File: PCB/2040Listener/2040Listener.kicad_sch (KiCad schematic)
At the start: 23 parts, among them J1 USB_B_Micro, J2 Conn_01x02, U1 NCP1117-3.3_SOT223, U2 BY25Q16AWTIG(R), U3 RP2040

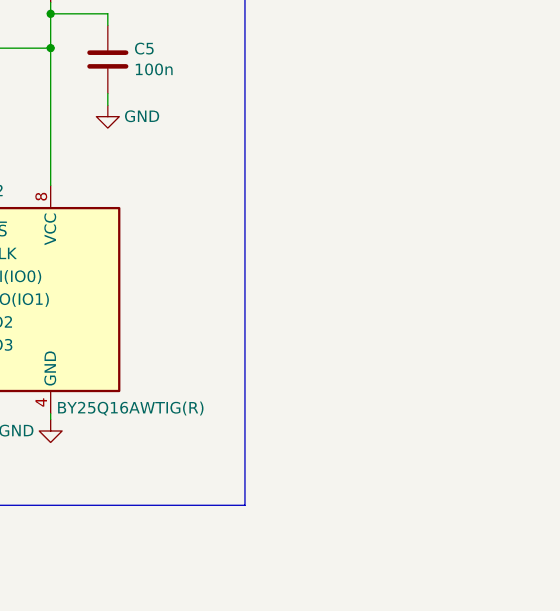
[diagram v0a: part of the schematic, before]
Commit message: change to 0805
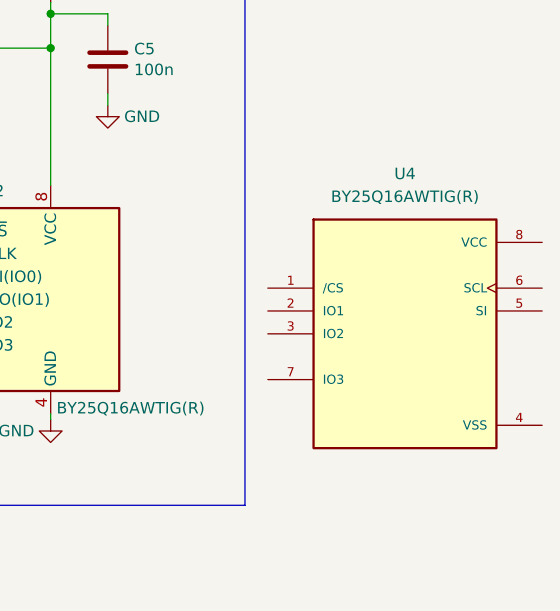
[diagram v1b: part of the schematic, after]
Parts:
- added U4: BY25Q16AWTIG(R), symbol SymbolLibrary:BY25Q16AWTIG(R)
- C10, C11, C12, C13, C14, C15, C16, C5, C6, C7, C8, C9: footprint Capacitor_SMD:C_0402_1005Metric -> Capacitor_SMD:C_0805_2012Metric
- R1, R2, R3, R4: footprint Resistor_SMD:R_0402_1005Metric -> Resistor_SMD:R_0805_2012Metric
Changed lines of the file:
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@@
 			)
 		)
-		(property "Footprint" "Resistor_SMD:R_0402_1005Metric"
+		(property "Footprint" "Resistor_SMD:R_0805_2012Metric"
 			(at 256.032 34.29 90)
 			(effects
@@
 			)
 		)
-		(property "Footprint" "Resistor_SMD:R_0402_1005Metric"
+		(property "Footprint" "Resistor_SMD:R_0805_2012Metric"
 			(at 242.57 47.752 90)
 			(effects
@@
 			)
 		)
-		(property "Footprint" "Capacitor_SMD:C_0402_1005Metric"
+		(property "Footprint" "Capacitor_SMD:C_0805_2012Metric"
 			(at 299.4152 34.29 0)
 			(effects
@@
 			)
 		)
-		(property "Footprint" "Resistor_SMD:R_0402_1005Metric"
+		(property "Footprint" "Resistor_SMD:R_0805_2012Metric"
 			(at 144.78 56.642 90)
 			(effects
@@
 			)
 		)
-		(property "Footprint" "Resistor_SMD:R_0402_1005Metric"
+		(property "Footprint" "Resistor_SMD:R_0805_2012Metric"
 			(at 144.78 64.262 90)
 			(effects
@@
 			)
 		)
-		(property "Footprint" "Capacitor_SMD:C_0402_1005Metric"
+		(property "Footprint" "Capacitor_SMD:C_0805_2012Metric"
 			(at 124.1552 31.75 0)
 			(effects
@@
 			)
 		)
-		(property "Footprint" "Capacitor_SMD:C_0402_1005Metric"
+		(property "Footprint" "Capacitor_SMD:C_0805_2012Metric"
 			(at 135.5852 31.75 0)
 			(effects
@@
 			)
 		)
-		(property "Footprint" "Capacitor_SMD:C_0402_1005Metric"
+		(property "Footprint" "Capacitor_SMD:C_0805_2012Metric"
 			(at 147.0152 31.75 0)
 			(effects
@@
 			)
 		)
-		(property "Footprint" "Capacitor_SMD:C_0402_1005Metric"
+		(property "Footprint" "Capacitor_SMD:C_0805_2012Metric"
 			(at 158.4452 31.75 0)
 			(effects
@@
 			)
 		)
-		(property "Footprint" "Capacitor_SMD:C_0402_1005Metric"
+		(property "Footprint" "Capacitor_SMD:C_0805_2012Metric"
 			(at 169.8752 31.75 0)
 			(effects
@@
 			)
 		)
-		(property "Footprint" "Capacitor_SMD:C_0402_1005Metric"
+		(property "Footprint" "Capacitor_SMD:C_0805_2012Metric"
 			(at 181.3052 31.75 0)
 			(effects
@@
 			)
 		)
-		(property "Footprint" "Capacitor_SMD:C_0402_1005Metric"
+		(property "Footprint" "Capacitor_SMD:C_0805_2012Metric"
 			(at 192.7352 31.75 0)
 			(effects
@@
 			)
 		)
-		(property "Footprint" "Capacitor_SMD:C_0402_1005Metric"
+		(property "Footprint" "Capacitor_SMD:C_0805_2012Metric"
 			(at 58.1152 31.75 0)
 			(effects
@@
 			)
 		)
-		(property "Footprint" "Capacitor_SMD:C_0402_1005Metric"
+		(property "Footprint" "Capacitor_SMD:C_0805_2012Metric"
 			(at 69.5452 31.75 0)
 			(effects
@@
 			)
 		)
-		(property "Footprint" "Capacitor_SMD:C_0402_1005Metric"
+		(property "Footprint" "Capacitor_SMD:C_0805_2012Metric"
 			(at 69.5452 46.99 0)
 			(effects
@@
 			)
 		)
-		(property "Footprint" "Capacitor_SMD:C_0402_1005Metric"
+		(property "Footprint" "Capacitor_SMD:C_0805_2012Metric"
 			(at 124.1552 46.99 0)
 			(effects
@@
 					(unit 1)
 				)
+			)
+		)
+	)
+	(symbol
+		(lib_id "SymbolLibrary:BY25Q16AWTIG(R)")
+		(at 331.47 60.96 0)
+		(unit 1)
+		(exclude_from_sim no)
+		(in_bom yes)
+		(on_board yes)
+		(dnp no)
+		(fields_autoplaced yes)
+		(property "Reference" "U4"
+			(at 331.47 43.18 0)
+			(effects
+				(font
+					(size 1.27 1.27)
+				)
+			)
+		)
+		(property "Value" "BY25Q16AWTIG(R)"
+			(at 331.47 45.72 0)
+			(effects
+				(font
+					(size 1.27 1.27)
+				)
+			)
+		)
+		(property "Footprint" ""
+			(at 331.47 60.96 0)
+			(effects
+				(font
+					(size 1.27 1.27)
+				)
+				(justify bottom)
+				(hide yes)
+			)
+		)
+		(property "Datasheet" ""
+			(at 331.47 60.96 0)
+			(effects
+				(font
+					(size 1.27 1.27)
+				)
+				(hide yes)
+			)
+		)
+		(property "Description" ""
+			(at 331.47 60.96 0)
+			(effects
+				(font
+					(size 1.27 1.27)
+				)
+				(hide yes)
+			)
+		)
+		(property "MAXIMUM_PACKAGE_HEIGHT" ""
+			(at 331.47 60.96 0)
+			(effects
+				(font
+					(size 1.27 1.27)
+				)
+				(justify bottom)
+				(hide yes)
+			)
+		)
+		(property "CREATOR" ""
+			(at 331.47 60.96 0)
+			(effects
+				(font
+					(size 1.27 1.27)
+				)
+				(justify bottom)
+				(hide yes)
+			)
+		)
+		(property "STANDARD" ""
+			(at 331.47 60.96 0)
+			(effects
+				(font
+					(size 1.27 1.27)
+				)
+				(justify bottom)
+				(hide yes)
+			)
+		)
+		(property "PARTREV" ""
+			(at 331.47 60.96 0)
+			(effects
+				(font
+					(size 1.27 1.27)
+				)
+				(justify bottom)
+				(hide yes)
+			)
+		)
+		(property "VERIFIER" ""
+			(at 331.47 60.96 0)
+			(effects
+				(font
+					(size 1.27 1.27)
+				)
+				(justify bottom)
+				(hide yes)
+			)
+		)
+		(property "MANUFACTURER" ""
+			(at 331.47 60.96 0)
+			(effects
+				(font
+					(size 1.27 1.27)
+				)
+				(justify bottom)
+				(hide yes)
+			)
+		)
+		(pin "3"
+		)
+		(pin "4"
+		)
+		(pin "1"
+		)
+		(pin "7"
+		)
+		(pin "6"
+		)
+		(pin "8"
+		)
+		(pin "2"
+		)
+		(pin "5"
+		)
+		(instances
+			(project ""
+				(path "/a808e31f-6f6f-4c04-a547-e5c681d45c47"
+					(reference "U4")
+					(unit 1)
+				)

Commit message: update pcb, symbols
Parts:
- removed J1: USB_B_Micro, RP2040_minimal:USB_Micro-B_Amphenol_10103594-0001LF_Horizontal_modified, symbol Connector:USB_B_Micro
- added C13: 15p, Diode_SMD:D_0805_2012Metric, symbol Device:C
- added C14: 15p, Capacitor_SMD:C_0402_1005Metric, symbol Device:C
- added C9: 10u, Capacitor_SMD:C_0805_2012Metric, symbol Device:C
- added J1: CONN4_292303_SOCKET, Library:CONN4_292303_TEC, symbol SymbolLibrary:CONN RCPT TYPEA 4POS R/A
- added J2: USB-AP-S-RA-PLUG, Library:CONN_USB-AP-S-RA-SMT_ADM, symbol SymbolLibrary:USB-AP-S-RA-SMT
- added R5: 1k, Resistor_SMD:R_0805_2012Metric, symbol Device:R
- added Y1: ABM8-272-T3, Crystal:Crystal_SMD_3225-4Pin_3.2x2.5mm, symbol Device:Crystal_GND24
- renumbered C6 to C1, C14 to C10, C15 to C11, C16 to C12, C1 to C15, C4 to C16, C5 to C17, C7 to C2, C8 to C3, C9 to C4, C10 to C5, C11 to C6, C12 to C7, C13 to C8, J2 to J3, R3 to R1, R4 to R2, R1 to R3, R2 to R4, U3 to U1, U1 to U2, U2 to U3
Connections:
- net +3V3: now also C9.1
- net GND: now also C13.2, C14.2, C9.2, J1.4 (GND), J2.4 (GND), Y1.2, Y1.4
- net GPIO0: now also J1.3 (D+)
- net GPIO1: now also J1.2 (D-)
- net USB_D+: now also J2.3 (D+)
- net USB_D-: now also J2.2 (D-)
- net VBUS: now also J1.1 (5V), J2.1 (5V)
- net XIN: now also C13.1, Y1.1
- net XOUT: now also R5.1
- net GPIO10: no longer names the net of U1.13 (GPIO10)
- net GPIO11: no longer names the net of U1.14 (GPIO11)
- net GPIO12: no longer names the net of U1.15 (GPIO12)
- net GPIO13: no longer names the net of U1.16 (GPIO13)
- net GPIO14: no longer names the net of U1.17 (GPIO14)
- net GPIO15: no longer names the net of U1.18 (GPIO15)
- net GPIO16: no longer names the net of U1.27 (GPIO16)
- net GPIO17: no longer names the net of U1.28 (GPIO17)
- net GPIO18: no longer names the net of U1.29 (GPIO18)
- net GPIO19: no longer names the net of U1.30 (GPIO19)
- net GPIO20: no longer names the net of U1.31 (GPIO20)
- net GPIO21: no longer names the net of U1.32 (GPIO21)
- net GPIO22: no longer names the net of U1.34 (GPIO22)
- net GPIO23: no longer names the net of U1.35 (GPIO23)
- net GPIO24: no longer names the net of U1.36 (GPIO24)
- net GPIO25: no longer names the net of U1.37 (GPIO25)
- net GPIO26_ADC0: no longer names the net of U1.38 (GPIO26_ADC0)
- net GPIO27_ADC1: no longer names the net of U1.39 (GPIO27_ADC1)
- net GPIO28_ADC2: no longer names the net of U1.40 (GPIO28_ADC2)
- net GPIO29_ADC3: no longer names the net of U1.41 (GPIO29_ADC3)
- net GPIO5: no longer names the net of U1.7 (GPIO5)
- net GPIO6: no longer names the net of U1.8 (GPIO6)
- net GPIO7: no longer names the net of U1.9 (GPIO7)
- net GPIO8: no longer names the net of U1.11 (GPIO8)
- net GPIO9: no longer names the net of U1.12 (GPIO9)
- new net: C14.1, R5.2, Y1.3
- no-connect marks 1 -> 0
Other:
- note added: "Crystal"
- note added: "USB"
- moved on the sheet: C15, C16, U2

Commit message: routing
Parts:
- removed J3: Conn_01x02, Connector_PinHeader_2.54mm:PinHeader_1x02_P2.54mm_Vertical, symbol Connector_Generic:Conn_01x02
- added R6: 1k, Resistor_SMD:R_0805_2012Metric, symbol Device:R
- added R7, R8: 27, Resistor_SMD:R_0805_2012Metric, symbol Device:R
- added SW1, SW2: PTS815 SJM 250 SMTR LFS, Library:SW4_PTS815 SJM 250 SMTR LFS_CNK, symbol SymbolLibrary:PTS815_SJM_250_SMTR_LFS
- U1: footprint RP2040_minimal:RP2040-QFN-56 -> Library:RP2040-QFN-56
- U4: footprint (none) -> Library:SOIC127P600X175-8N
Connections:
- net +3V3: now also SW2.4
- net GND: now also R6.2, SW1.3
- net GPIO0: now also R7.1; no longer U1.2 (GPIO0)
- net GPIO1: now also R8.1; no longer U1.3 (GPIO1)
- net GPIO17: now reaches U1.28 (GPIO17)
- net GPIO17: now also SW2.2
- net GPIO2: no longer names the net of U1.4 (GPIO2)
- net GPIO3: no longer names the net of U1.5 (GPIO3)
- net GPIO4: no longer names the net of U1.6 (GPIO4)
- net ~{USB_BOOT}: no longer names the net of R3.2
- net ~{USB_BOOT}: now also SW1.2
- new net: R7.2, U1.2 (GPIO0)
- new net: R8.2, U1.3 (GPIO1)
- new net: R6.1, SW2.1
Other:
- note added: "CDC Toggle"
- moved on the sheet: R3, R4

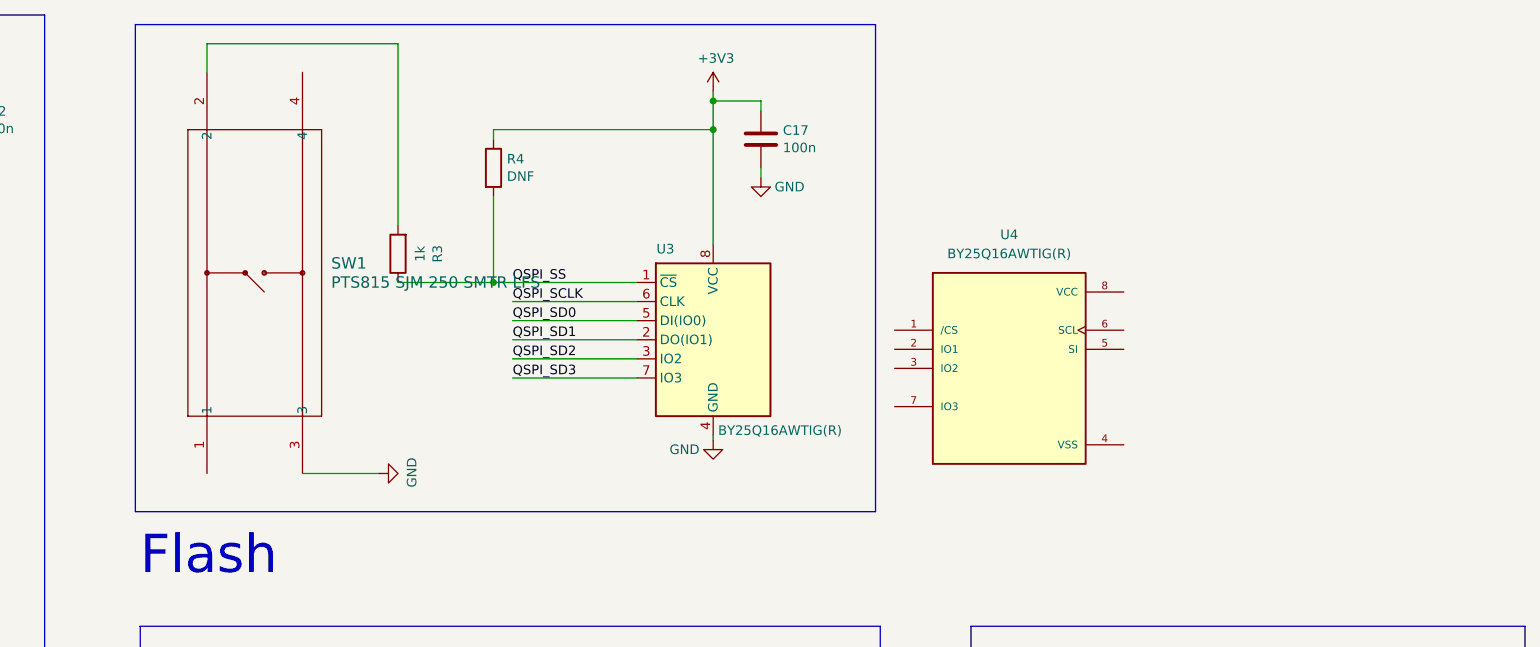
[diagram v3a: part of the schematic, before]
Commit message: reposition elements for better routing
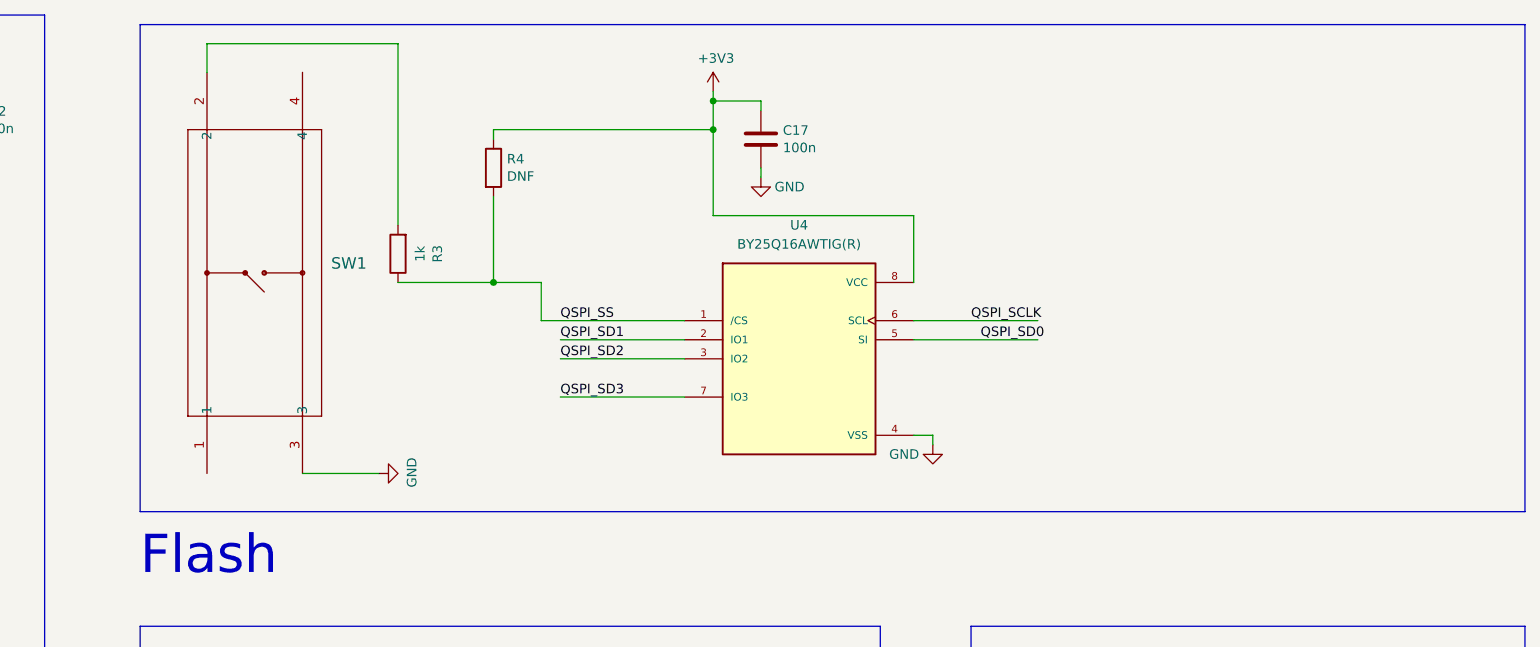
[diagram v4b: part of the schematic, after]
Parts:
- removed U3: BY25Q16AWTIG(R), Package_SO:SOIC-8_5.23x5.23mm_P1.27mm, symbol Memory_Flash:W25Q128JVS
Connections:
- net +3V3: now also U4.8 (VCC)
- net GND: now also U4.4 (VSS)
- net QSPI_SCLK: now also U4.6 (SCL)
- net QSPI_SD0: now also U4.5 (SI)
- net QSPI_SD1: now also U4.2 (IO1)
- net QSPI_SD2: now also U4.3 (IO2)
- net QSPI_SD3: now also U4.7 (IO3)
- net QSPI_SS: now also U4.1 (/CS)
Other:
- moved on the sheet: U4
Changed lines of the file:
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@@
 	(paper "A3")
 	(rectangle
-		(start 215.265 15.24)
-		(end 313.69 80.01)
+		(start 215.9 15.24)
+		(end 400.05 80.01)
 		(stroke
 			(width 0)
@@
 	(wire
 		(pts
-			(xy 281.94 59.69) (xy 265.43 59.69)
+			(xy 288.29 59.69) (xy 271.78 59.69)
 		)
 		(stroke
@@
 	(wire
 		(pts
-			(xy 265.43 52.07) (xy 281.94 52.07)
+			(xy 321.31 69.85) (xy 318.77 69.85)
 		)
 		(stroke
@@
 	(wire
 		(pts
-			(xy 281.94 57.15) (xy 265.43 57.15)
+			(xy 288.29 57.15) (xy 271.78 57.15)
 		)
 		(stroke
@@
 	(wire
 		(pts
+			(xy 318.77 54.61) (xy 335.28 54.61)
+		)
+		(stroke
+			(width 0)
+			(type default)
+		)
+	)
+	(wire
+		(pts
 			(xy 237.49 115.57) (xy 247.65 115.57)
 		)
@@
 	(wire
 		(pts
-			(xy 262.89 49.53) (xy 281.94 49.53)
+			(xy 269.24 54.61) (xy 288.29 54.61)
 		)
 		(stroke
@@
 	(wire
 		(pts
+			(xy 292.1 40.64) (xy 318.77 40.64)
+		)
+		(stroke
+			(width 0)
+			(type default)
+		)
+	)
+	(wire
+		(pts
 			(xy 66.04 138.43) (xy 52.07 138.43)
 		)
@@
 	(wire
 		(pts
-			(xy 281.94 54.61) (xy 265.43 54.61)
-		)
-		(stroke
-			(width 0)
-			(type default)
-		)
-	)
-	(wire
-		(pts
 			(xy 104.14 55.88) (xy 104.14 43.18)
 		)
@@
 	(wire
 		(pts
-			(xy 281.94 62.23) (xy 265.43 62.23)
+			(xy 288.29 64.77) (xy 271.78 64.77)
 		)
 		(stroke
@@
 	(wire
 		(pts
-			(xy 292.1 70.485) (xy 292.1 69.85)
+			(xy 321.31 69.85) (xy 321.31 71.12)
 		)
 		(stroke
@@
 	(wire
 		(pts
+			(xy 318.77 40.64) (xy 318.77 49.53)
+		)
+		(stroke
+			(width 0)
+			(type default)
+		)
+	)
+	(wire
+		(pts
 			(xy 57.15 33.02) (xy 57.15 34.29)
 		)
@@
 	(wire
 		(pts
+			(xy 318.77 57.15) (xy 335.28 57.15)
+		)
+		(stroke
+			(width 0)
+			(type default)
+		)
+	)
+	(wire
+		(pts
 			(xy 250.19 49.53) (xy 262.89 49.53)
 		)
@@
 	(wire
 		(pts
-			(xy 292.1 29.21) (xy 292.1 44.45)
+			(xy 292.1 29.21) (xy 292.1 40.64)
 		)
 		(stroke
@@
 	(wire
 		(pts
+			(xy 269.24 54.61) (xy 269.24 49.53)
+		)
+		(stroke
+			(width 0)
+			(type default)
+		)
+	)
+	(wire
+		(pts
+			(xy 269.24 49.53) (xy 262.89 49.53)
+		)
+		(stroke
+			(width 0)
+			(type default)
+		)
+	)
+	(wire
+		(pts
 			(xy 104.14 229.87) (xy 96.52 229.87)
 		)
@@
 	)
 	(label "QSPI_SD2"
-		(at 265.43 59.69 0)
+		(at 271.78 59.69 0)
 		(effects
 			(font
@@
 	)
 	(label "QSPI_SD3"
-		(at 265.43 62.23 0)
+		(at 271.78 64.77 0)
 		(effects
 			(font
@@
 	)
 	(label "QSPI_SD0"
-		(at 265.43 54.61 0)
+		(at 327.66 57.15 0)
 		(effects
 			(font
@@
 	)
 	(label "QSPI_SCLK"
-		(at 265.43 52.07 0)
+		(at 326.39 54.61 0)
 		(effects
 			(font
@@
 	)
 	(label "QSPI_SS"
-		(at 265.43 49.53 0)
+		(at 271.78 54.61 0)
 		(effects
 			(font
@@
 	)
 	(label "QSPI_SD1"
-		(at 265.43 57.15 0)
+		(at 271.78 57.15 0)
 		(effects
 			(font
@@
 	)
 	(symbol
-		(lib_id "Memory_Flash:W25Q128JVS")
-		(at 292.1 57.15 0)
-		(unit 1)
-		(exclude_from_sim no)
-		(in_bom yes)
-		(on_board yes)
-		(dnp no)
-		(property "Reference" "U3"
-			(at 285.75 45.085 0)
-			(effects
-				(font
-					(size 1.27 1.27)
-				)
-			)
-		)
-		(property "Value" "BY25Q16AWTIG(R)"
-			(at 300.99 69.215 0)
-			(effects
-				(font
-					(size 1.27 1.27)
-				)
-			)
-		)
-		(property "Footprint" "Package_SO:SOIC-8_5.23x5.23mm_P1.27mm"
-			(at 292.1 57.15 0)
-			(effects
-				(font
-					(size 1.27 1.27)
-				)
-				(hide yes)
-			)
-		)
-		(property "Datasheet" "http://www.winbond.com/resource-files/w25q128jv_dtr%20revc%2003272018%20plus.pdf"
-			(at 292.1 57.15 0)
-			(effects
-				(font
-					(size 1.27 1.27)
-				)
-				(hide yes)
-			)
-		)
-		(property "Description" ""
-			(at 292.1 57.15 0)
-			(effects
-				(font
-					(size 1.27 1.27)
-				)
-			)
-		)
-		(pin "1"
-		)
-		(pin "2"
-		)
-		(pin "3"
-		)
-		(pin "4"
-		)
-		(pin "5"
-		)
-		(pin "6"
-		)
-		(pin "7"
-		)
-		(pin "8"
-		)
-		(instances
-			(project "2040Listener"
-				(path "/a808e31f-6f6f-4c04-a547-e5c681d45c47"
-					(reference "U3")
-					(unit 1)
-				)
-			)
-		)
-	)
-	(symbol
 		(lib_id "power:+3V3")
 		(at 292.1 24.13 0)
@@
 	(symbol
 		(lib_id "power:GND")
-		(at 292.1 70.485 0)
+		(at 321.31 71.12 0)
 		(unit 1)
 		(exclude_from_sim no)
@@
 		(dnp no)
 		(property "Reference" "#PWR025"
-			(at 292.1 76.835 0)
+			(at 321.31 77.47 0)
 			(effects
 				(font
@@
 		)
 		(property "Value" "GND"
-			(at 288.29 71.755 0)
+			(at 317.5 72.39 0)
 			(effects
 				(font
@@
 		)
 		(property "Footprint" ""
-			(at 292.1 70.485 0)
+			(at 321.31 71.12 0)
 			(effects
 				(font
@@
 		)
 		(property "Datasheet" ""
-			(at 292.1 70.485 0)
+			(at 321.31 71.12 0)
 			(effects
 				(font
@@
 		)
 		(property "Description" ""
-			(at 292.1 70.485 0)
+			(at 321.31 71.12 0)
 			(effects
 				(font
@@
 	(symbol
 		(lib_id "SymbolLibrary:BY25Q16AWTIG(R)")
-		(at 331.47 60.96 0)
+		(at 303.53 59.69 0)
 		(unit 1)
 		(exclude_from_sim no)
@@
 		(fields_autoplaced yes)
 		(property "Reference" "U4"
-			(at 331.47 43.18 0)
+			(at 303.53 41.91 0)
 			(effects
 				(font
@@
 		)
 		(property "Value" "BY25Q16AWTIG(R)"
-			(at 331.47 45.72 0)
+			(at 303.53 44.45 0)
 			(effects
 				(font
@@
 		)
 		(property "Footprint" "Library:SOIC127P600X175-8N"
-			(at 331.47 60.96 0)
+			(at 303.53 59.69 0)
 			(effects
 				(font
@@
 		)
 		(property "Datasheet" ""
-			(at 331.47 60.96 0)
+			(at 303.53 59.69 0)
 			(effects
 				(font
@@
 		)
 		(property "Description" ""
-			(at 331.47 60.96 0)
+			(at 303.53 59.69 0)
 			(effects
 				(font
@@
 		)
 		(property "MAXIMUM_PACKAGE_HEIGHT" ""
-			(at 331.47 60.96 0)
+			(at 303.53 59.69 0)
 			(effects
 				(font
@@
 		)
 		(property "CREATOR" ""
-			(at 331.47 60.96 0)
+			(at 303.53 59.69 0)
 			(effects
 				(font
@@
 		)
 		(property "STANDARD" ""
-			(at 331.47 60.96 0)
+			(at 303.53 59.69 0)
 			(effects
 				(font
@@
 		)
 		(property "PARTREV" ""
-			(at 331.47 60.96 0)
+			(at 303.53 59.69 0)
 			(effects
 				(font
@@
 		)
 		(property "VERIFIER" ""
-			(at 331.47 60.96 0)
+			(at 303.53 59.69 0)
 			(effects
 				(font
@@
 		)
 		(property "MANUFACTURER" ""
-			(at 331.47 60.96 0)
+			(at 303.53 59.69 0)
 			(effects
 				(font
@@
 		(on_board yes)
 		(dnp no)
-		(fields_autoplaced yes)
 		(property "Reference" "SW1"
 			(at 241.3 46.9899 90)
@@
 		)
 		(property "Value" "PTS815 SJM 250 SMTR LFS"
-			(at 241.3 49.5299 90)
+			(at 240.792 55.626 90)
 			(effects
 				(font
@@
 				)
 				(justify right)
+				(hide yes)
 			)
 		)

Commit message: fix small footprint
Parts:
- C14: footprint Capacitor_SMD:C_0402_1005Metric -> Capacitor_SMD:C_0805_2012Metric
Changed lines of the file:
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@@
 			)
 		)
-		(property "Footprint" "Capacitor_SMD:C_0402_1005Metric"
+		(property "Footprint" "Capacitor_SMD:C_0805_2012Metric"
 			(at 236.22 194.0052 0)
 			(effects
